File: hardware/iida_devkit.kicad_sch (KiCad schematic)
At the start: 9 parts

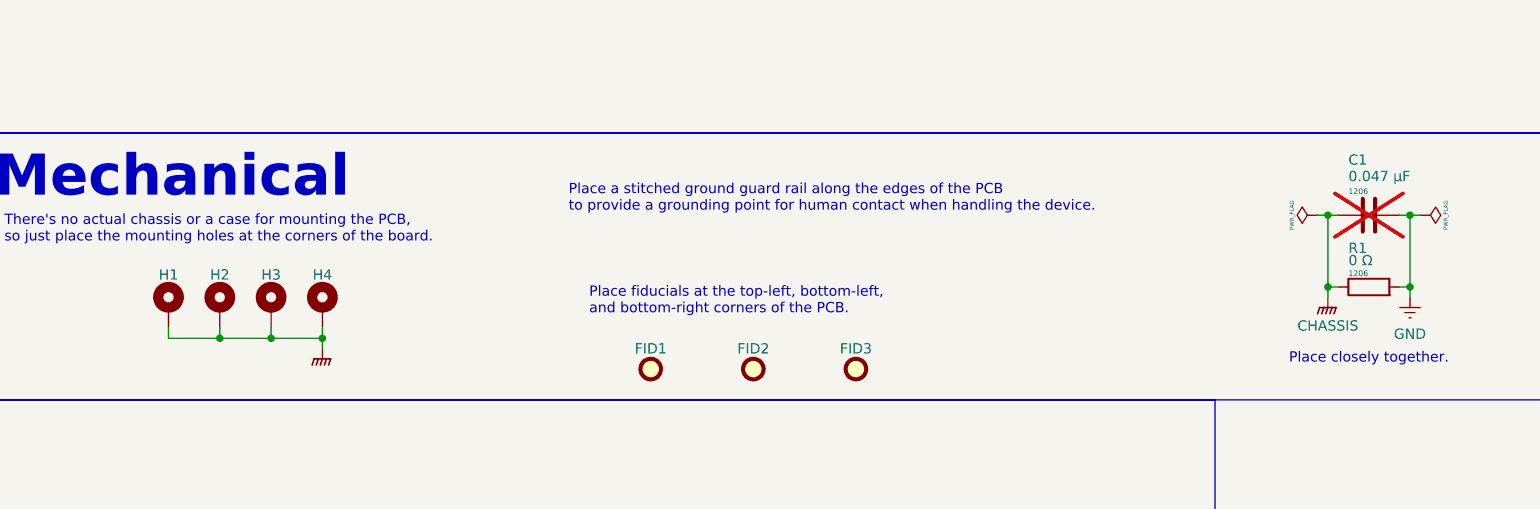
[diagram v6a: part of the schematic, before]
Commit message: HW: BAT_DETn -> USB_DET
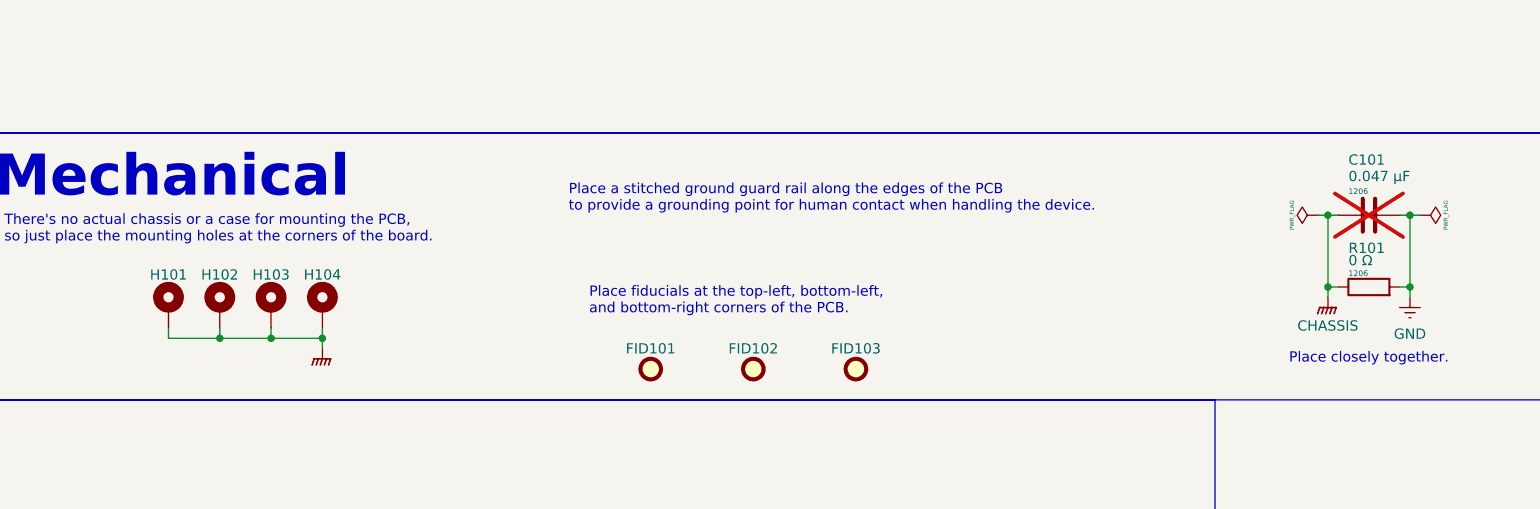
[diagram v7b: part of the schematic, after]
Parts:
- renumbered C1 to C101, FID1 to FID101, FID2 to FID102, FID3 to FID103, H1 to H101, H2 to H102, H3 to H103, H4 to H104, R1 to R101
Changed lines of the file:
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@@
 		(in_pos_files yes)
 		(dnp no)
-		(property "Reference" "#FLG02"
+		(property "Reference" "#FLG0102"
 			(at 325.755 228.6 0)
 			(hide yes)
@@
 			(project "iida_devkit"
 				(path "/b12a6e25-97fb-4aba-bc96-af8db389bb9a"
-					(reference "#FLG02")
+					(reference "#FLG0102")
 					(unit 1)
 				)
@@
 		(in_pos_files yes)
 		(dnp no)
-		(property "Reference" "H1"
+		(property "Reference" "H101"
 			(at 168.91 236.728 0)
 			(show_name no)
@@
 			(project "iida_devkit"
 				(path "/b12a6e25-97fb-4aba-bc96-af8db389bb9a"
-					(reference "H1")
+					(reference "H101")
 					(unit 1)
 				)
@@
 		(in_pos_files yes)
 		(dnp no)
-		(property "Reference" "H4"
+		(property "Reference" "H104"
 			(at 187.96 236.728 0)
 			(show_name no)
@@
 			(project "iida_devkit"
 				(path "/b12a6e25-97fb-4aba-bc96-af8db389bb9a"
-					(reference "H4")
+					(reference "H104")
 					(unit 1)
 				)
@@
 		(in_pos_files yes)
 		(dnp no)
-		(property "Reference" "FID2"
+		(property "Reference" "FID102"
 			(at 241.3 245.872 0)
 			(show_name no)
@@
 			(project "iida_devkit"
 				(path "/b12a6e25-97fb-4aba-bc96-af8db389bb9a"
-					(reference "FID2")
+					(reference "FID102")
 					(unit 1)
 				)
@@
 		(in_pos_files yes)
 		(dnp no)
-		(property "Reference" "H2"
+		(property "Reference" "H102"
 			(at 175.26 236.728 0)
 			(show_name no)
@@
 			(project "iida_devkit"
 				(path "/b12a6e25-97fb-4aba-bc96-af8db389bb9a"
-					(reference "H2")
+					(reference "H102")
 					(unit 1)
 				)
@@
 		(in_pos_files yes)
 		(dnp no)
-		(property "Reference" "#PWR04"
+		(property "Reference" "#PWR0104"
 			(at 322.58 245.11 0)
 			(hide yes)
@@
 			(project "iida_devkit"
 				(path "/b12a6e25-97fb-4aba-bc96-af8db389bb9a"
-					(reference "#PWR04")
+					(reference "#PWR0104")
 					(unit 1)
 				)
@@
 		(in_pos_files yes)
 		(dnp no)
-		(property "Reference" "FID1"
+		(property "Reference" "FID101"
 			(at 228.6 245.872 0)
 			(show_name no)
@@
 			(project "iida_devkit"
 				(path "/b12a6e25-97fb-4aba-bc96-af8db389bb9a"
-					(reference "FID1")
+					(reference "FID101")
 					(unit 1)
 				)
@@
 		(in_pos_files yes)
 		(dnp yes)
-		(property "Reference" "C1"
+		(property "Reference" "C101"
 			(at 314.96 222.504 90)
 			(show_name no)
@@
 			(project "iida_devkit"
 				(path "/b12a6e25-97fb-4aba-bc96-af8db389bb9a"
-					(reference "C1")
+					(reference "C101")
 					(unit 1)
 				)
@@
 		(in_pos_files yes)
 		(dnp no)
-		(property "Reference" "#PWR02"
+		(property "Reference" "#PWR0102"
 			(at 242.57 68.58 0)
 			(hide yes)
@@
 			(project "iida_devkit"
 				(path "/b12a6e25-97fb-4aba-bc96-af8db389bb9a"
-					(reference "#PWR02")
+					(reference "#PWR0102")
 					(unit 1)
 				)
@@
 		(in_pos_files yes)
 		(dnp no)
-		(property "Reference" "#FLG01"
+		(property "Reference" "#FLG0101"
 			(at 309.245 228.6 0)
 			(hide yes)
@@
 			(project "iida_devkit"
 				(path "/b12a6e25-97fb-4aba-bc96-af8db389bb9a"
-					(reference "#FLG01")
+					(reference "#FLG0101")
 					(unit 1)
 				)
@@
 		(in_pos_files yes)
 		(dnp no)
-		(property "Reference" "#PWR01"
+		(property "Reference" "#PWR0101"
 			(at 187.96 250.19 0)
 			(hide yes)
@@
 			(project "iida_devkit"
 				(path "/b12a6e25-97fb-4aba-bc96-af8db389bb9a"
-					(reference "#PWR01")
+					(reference "#PWR0101")
 					(unit 1)
 				)
@@
 		(in_pos_files yes)
 		(dnp no)
-		(property "Reference" "#PWR03"
+		(property "Reference" "#PWR0103"
 			(at 312.42 243.84 0)
 			(hide yes)
@@
 			(project "iida_devkit"
 				(path "/b12a6e25-97fb-4aba-bc96-af8db389bb9a"
-					(reference "#PWR03")
+					(reference "#PWR0103")
 					(unit 1)
 				)
@@
 		(in_pos_files yes)
 		(dnp no)
-		(property "Reference" "FID3"
+		(property "Reference" "FID103"
 			(at 254 245.872 0)
 			(show_name no)
@@
 			(project "iida_devkit"
 				(path "/b12a6e25-97fb-4aba-bc96-af8db389bb9a"
-					(reference "FID3")
+					(reference "FID103")
 					(unit 1)
 				)
@@
 		(in_pos_files yes)
 		(dnp no)
-		(property "Reference" "R1"
+		(property "Reference" "R101"
 			(at 314.96 233.426 90)
 			(show_name no)
@@
 			(project "iida_devkit"
 				(path "/b12a6e25-97fb-4aba-bc96-af8db389bb9a"
-					(reference "R1")
+					(reference "R101")
 					(unit 1)
 				)
@@
 		(in_pos_files yes)
 		(dnp no)
-		(property "Reference" "H3"
+		(property "Reference" "H103"
 			(at 181.61 236.728 0)
 			(show_name no)
@@
 			(project "iida_devkit"
 				(path "/b12a6e25-97fb-4aba-bc96-af8db389bb9a"
-					(reference "H3")
-					(unit 1)
-				)
+					(reference "H103")
+					(unit 1)
+				)

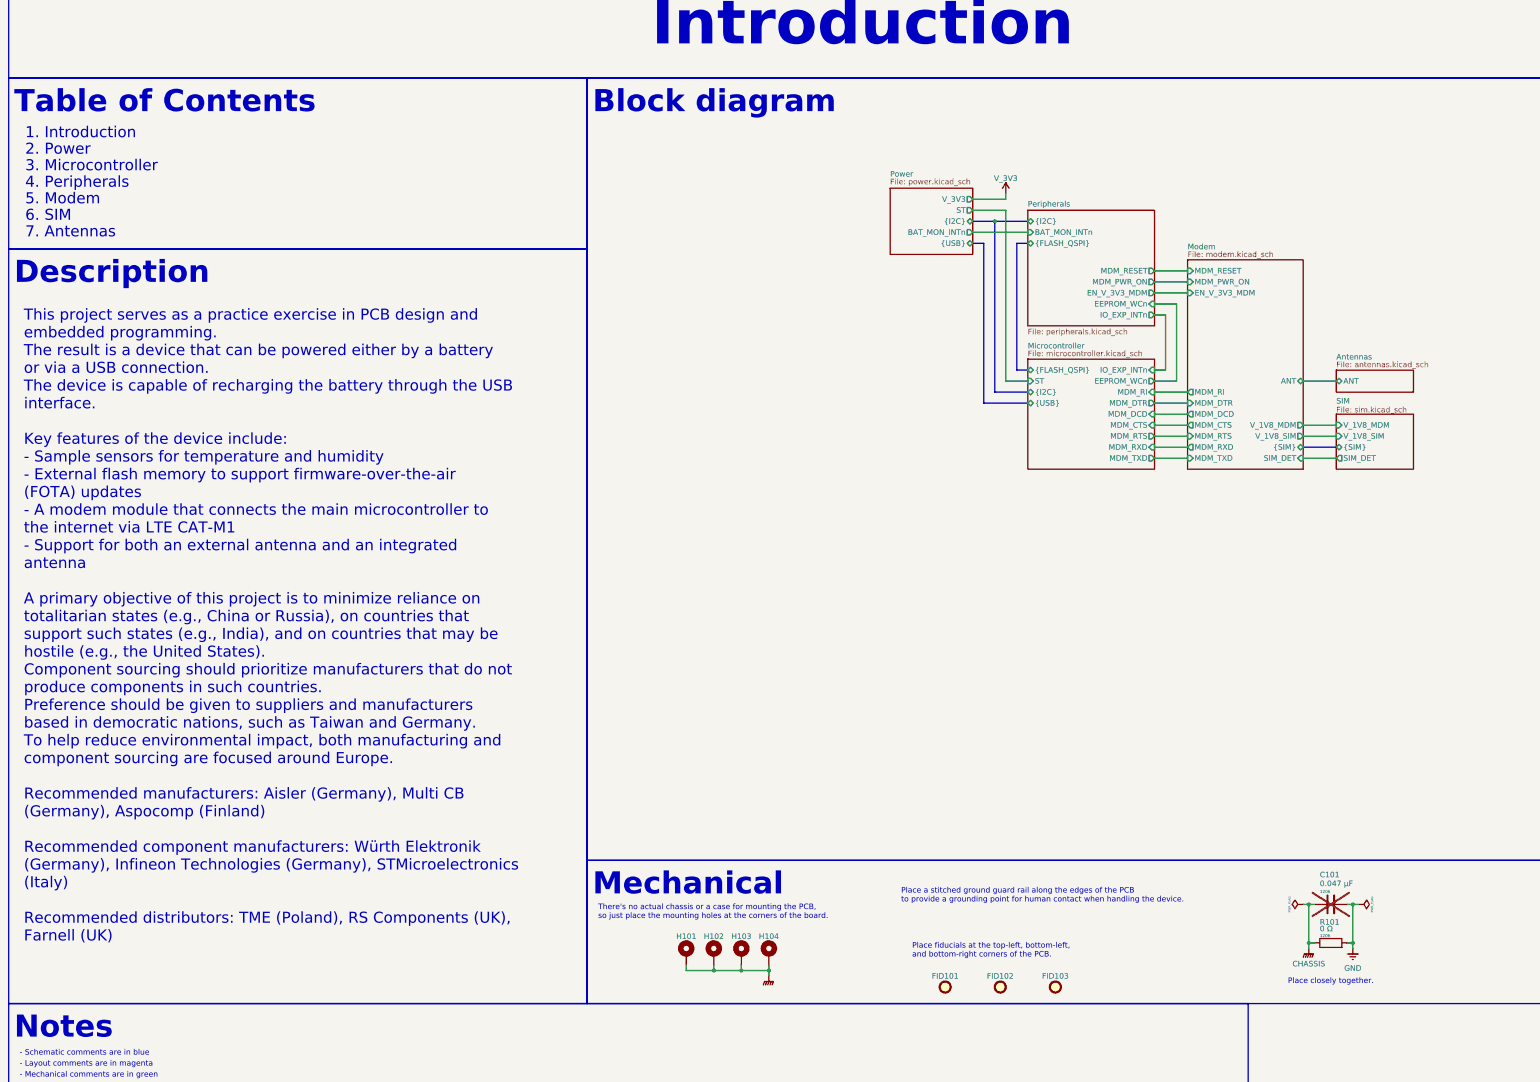
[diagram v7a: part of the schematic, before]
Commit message: HW: Move SIM to Modem
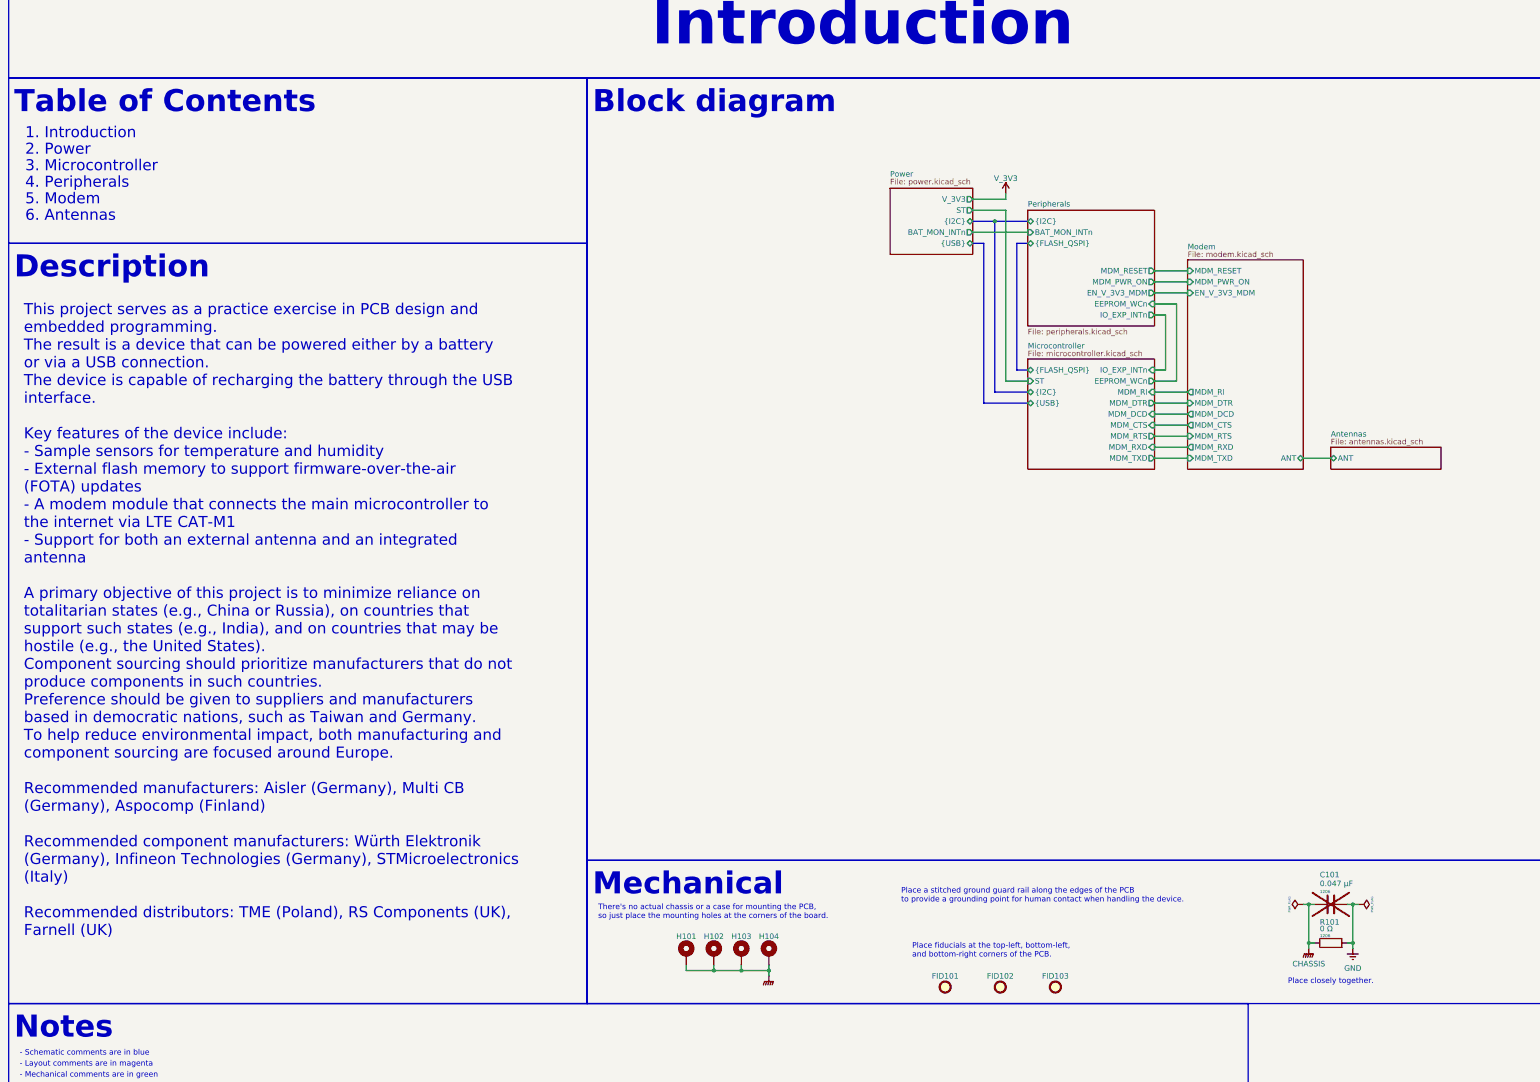
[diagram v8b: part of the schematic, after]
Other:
- removed sheet SIM
- sheet Modem ports: added none; removed SIM_DET, V_1V8_MDM, V_1V8_SIM, {SIM}
- note added: "6. Antennas"
- note removed: "6. SIM"
- note removed: "7. Antennas"
